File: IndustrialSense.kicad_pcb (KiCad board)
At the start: 4 copper layers, 46.9 x 90 mm, 111 parts, among them CN2 B4B-ZR (LF)(SN), CN3 ZH1.5-6P-LT, CN4 B4B-ZR (LF)(SN), J1 Conn_01x06_Socket, J3 Conn_01x06_Socket, J5 Conn_01x10_Socket, J6 Conn_01x10_Socket, Q1 SISA14DN-T1-GE3, Q13 MMBT3904, Q15 LMBT3904DW1T1G, Q2 SISA14DN-T1-GE3, Q3 SISA14DN-T1-GE3, Q4 SISA14DN-T1-GE3, Q5 CEM4435A, Q6 CH221K, SW2 SKRKAEE020, SW3 SKRKAEE020, U1 ESP32-S3-WROOM-1U-N16, U10 LM74700QDBVRQ1, U11 CN3795, U12 XFL4020-222MEC_C122469, U14 CH334F, U15 TPS3831G33DQNR, U17 THVD1406DR, U3 CH343P, U4 MAX17049G+T10, U5 LM74700QDBVRQ1, U6 LM74700QDBVRQ1, U7 TPS62132RGTT, U8 LM74700QDBVRQ1, U9 XC6209F332MR-G, X1 X322512MSB4SI

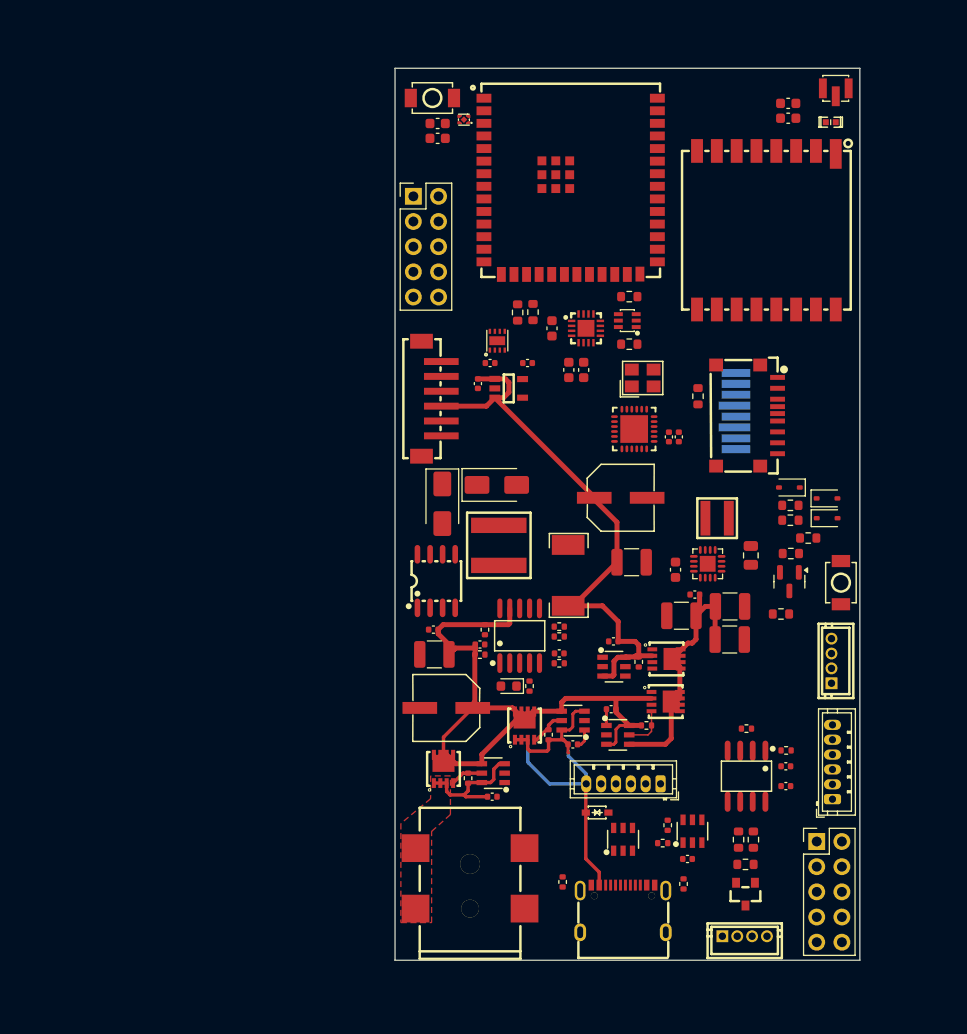
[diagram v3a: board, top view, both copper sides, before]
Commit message: [Schematic/PCB][Added] Routing almost finished
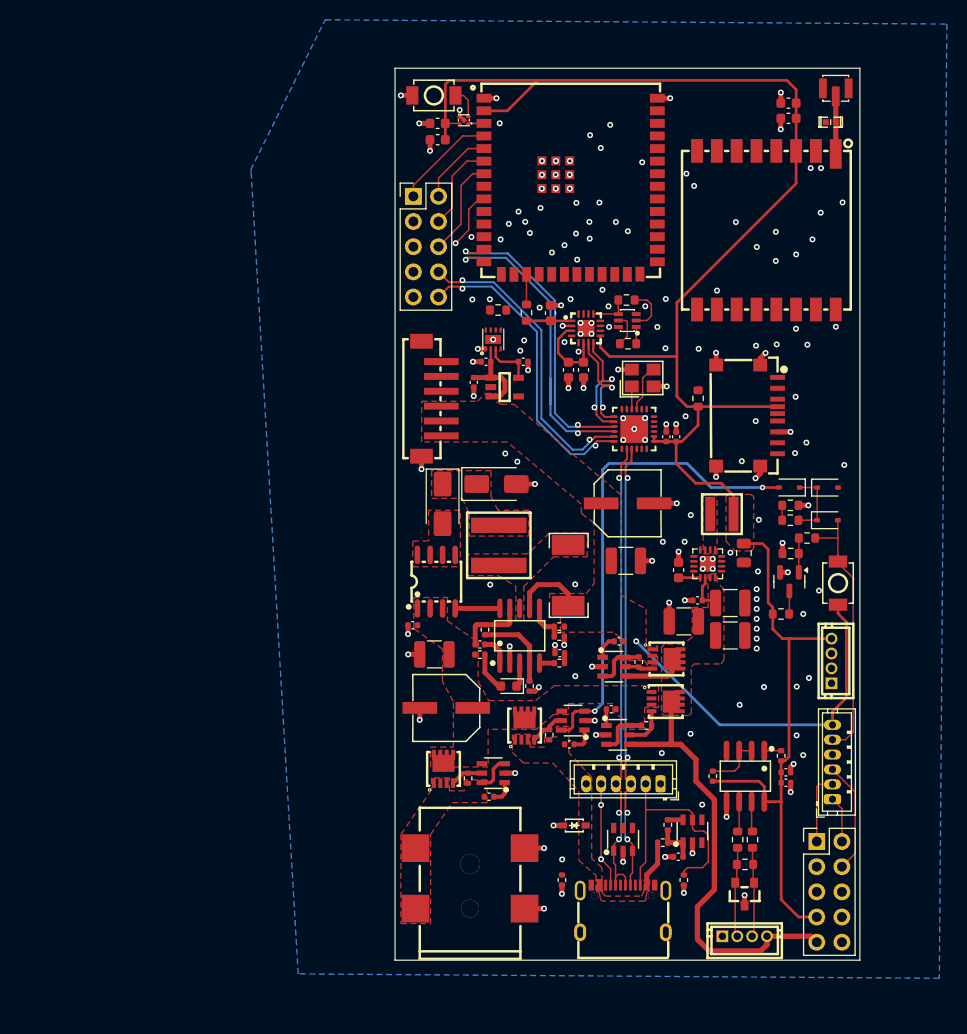
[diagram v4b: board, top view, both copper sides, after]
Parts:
- removed REF**: Micro_SD_Card, Library:microSD_card
- moved R19 5.88 mm to (156.6, 118.6), turned to 90 degrees
- moved D8 3.09 mm to (168.2, 89.5)
- moved D4 2.64 mm to (142.6, 123.6), turned to 0 degrees
- moved D7 2.20 mm to (168.1, 92.8)
- moved C22 2.13 mm to (126.3, 103.4)
- moved R58 1.99 mm to (134.9, 71.6), turned to 180 degrees
- moved C47 1.55 mm to (140.2, 71.9), turned to 90 degrees
- moved C37 0.96 mm to (153.1, 126.8), turned to 180 degrees
- moved C7 0.90 mm to (148.0, 91.1)
- moved C13 0.74 mm to (159.7, 96.1)
- moved R18 0.74 mm to (163.5, 116.6), turned to 90 degrees
- moved R57 0.66 mm to (137.8, 71.9)
- moved C15 0.65 mm to (155.0, 100.9)
- moved U12 0.63 mm to (157.5, 92.2)
- moved C6 0.62 mm to (153.7, 103.0)
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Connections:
- D7 pad 2: /Project Architecture/Power Management/KEY_PWR -> KEY_PWR
- J3 pad 5: /Project Architecture/External Connectors/PWR_KEY -> KEY_PWR
- J5 pad 3: /Project Architecture/External Connectors/PWR_KEY -> /Project Architecture/External Connectors/GPIO15
- J5 pad 5: /Project Architecture/External Connectors/GPIO15 -> /Project Architecture/External Connectors/GPIO16
- J5 pad 6: /Project Architecture/External Connectors/GPIO16 -> GND
- R48 pad 1: /Project Architecture/Power Management/KEY_PWR -> KEY_PWR
- SW2 pad 1: /Project Architecture/Power Management/KEY_PWR -> KEY_PWR
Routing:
- net 3V3_MCU: track 0.00 -> 186.0 mm
- net GND: track 0.00 -> 67.1 mm, vias 0 -> 95
- net V_CHRG: track 66.8 -> 13.0 mm
- net /Project Architecture/External Connectors/USBCD-: track 0.00 -> 47.7 mm, vias 0 -> 4
- net /Project Architecture/External Connectors/USBCD+: track 0.00 -> 45.6 mm, vias 0 -> 4
- net /Project Architecture/HUB/ESP_USBD-: track 0.00 -> 36.6 mm, vias 0 -> 2
- net /Project Architecture/HUB/ESP_USBD+: track 0.00 -> 36.6 mm, vias 0 -> 2
- net /Project Architecture/External Connectors/LTE_USBD-: track 0.00 -> 31.3 mm, vias 0 -> 2
- net /Project Architecture/External Connectors/LTE_USBD+: track 0.00 -> 31.3 mm, vias 0 -> 2
- net V_MAIN: track 26.1 -> 55.2 mm
- net KEY_PWR: track 0.00 -> 27.5 mm
- net /Project Architecture/External Connectors/CC2: track 0.00 -> 24.6 mm
- net VBUS: track 37.1 -> 53.4 mm, vias 0 -> 2
- net /Project Architecture/HUB/CH343_USBD-: track 0.00 -> 12.2 mm, vias 0 -> 2
- net /Project Architecture/HUB/CH343_USBD+: track 0.00 -> 11.4 mm, vias 0 -> 2
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- added copper zone on F.Cu, net 3V3_MCU
- added copper zone on B.Cu, net GND
- added copper zone on F.Cu, net Net-(D1-K)
- added copper zone on F.Cu, net Net-(D2-A)
- added copper zone on F.Cu, net Net-(U11-CSP)
- added copper zone on F.Cu, net Net-(U12-Pad1)
- added copper zone on F.Cu, net VBUS
- added copper zone on F.Cu, net V_BAT
- added copper zone on F.Cu, net V_CHRG
- added copper zone on F.Cu, net V_MAIN

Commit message: [Schematic/PCB][Added] Routing finished, DRC finished
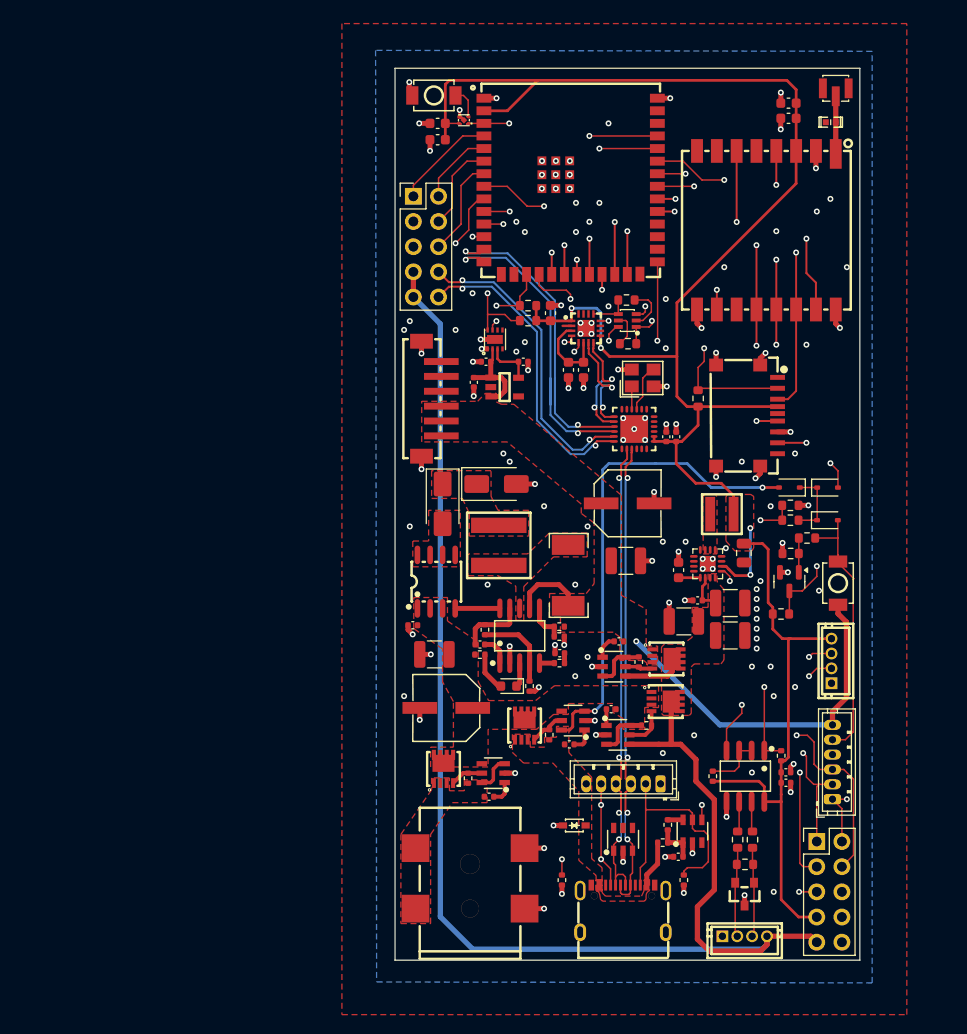
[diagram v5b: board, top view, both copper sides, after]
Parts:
- removed J1, J3: Conn_01x06_Socket, Connector_JST:JST_ZH_B6B-ZR_1x06_P1.50mm_Vertical
- added U13: B6B-ZR (LF)(SN), easyeda2kicad:CONN-TH-6P-P1.50_B6B-ZR-LF-SN, F.Cu at (147.6, 119.4)
- added U2: B6B-ZR (LF)(SN), easyeda2kicad:CONN-TH-6P-P1.50_B6B-ZR-LF-SN, F.Cu at (168.7, 117.2)
- moved R58 3.20 mm to (137.9, 72.7)
- moved R57 0.73 mm to (137.9, 71.2), turned to 180 degrees
- moved U4 0.18 mm to (134.6, 74.6)
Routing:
- net /Project Architecture/External Connectors/GPIO16: track 5.94 -> 118.2 mm, vias 1 -> 7
- net /Project Architecture/External Connectors/GPIO15: track 0.00 -> 104.6 mm, vias 2 -> 7
- net V_MAIN: track 55.2 -> 156.8 mm
- net /Project Architecture/External Connectors/I2C_SCL: track 3.04 -> 93.8 mm, vias 1 -> 7
- net /Project Architecture/External Connectors/I2C_SDA: track 0.01 -> 89.3 mm
- net /Project Architecture/MCU/RS485_RXD1: track 1.70 -> 89.8 mm
- net /Project Architecture/External Connectors/GPIO42R: track 4.66 -> 88.5 mm, vias 1 -> 4
- net /Project Architecture/External Connectors/GPIO41G: track 7.23 -> 89.1 mm, vias 6 -> 5
- net /Project Architecture/MCU/RS485_TXD1: track 0.00 -> 81.1 mm
- net /Project Architecture/External Connectors/GPIO40B: track 11.4 -> 87.6 mm, vias 4 -> 3
- net /Project Architecture/MCU/PWR_KEY: track 2.34 -> 58.6 mm, vias 0 -> 3
- net /Project Architecture/MCU/LOCK_PWR: track 0.00 -> 46.9 mm, vias 2 -> 3
- net /Project Architecture/LoRa/SPI_MISO/D0: track 0.00 -> 46.0 mm
- net /Project Architecture/LoRa/SPI_MOSI/CMD: track 0.00 -> 43.1 mm, vias 4 -> 2
- net /Project Architecture/MCU/ESP_TXD0: track 0.00 -> 43.0 mm
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- added copper zone on F.Cu, net GND

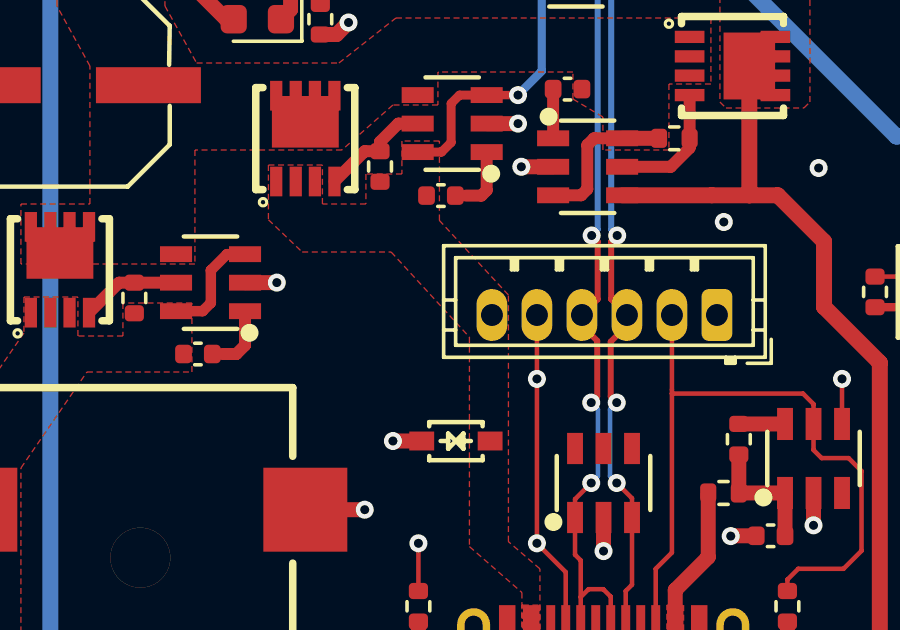
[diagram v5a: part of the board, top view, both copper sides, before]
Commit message: [Schematic/PCB][Added] Testpoints and fabrication files test
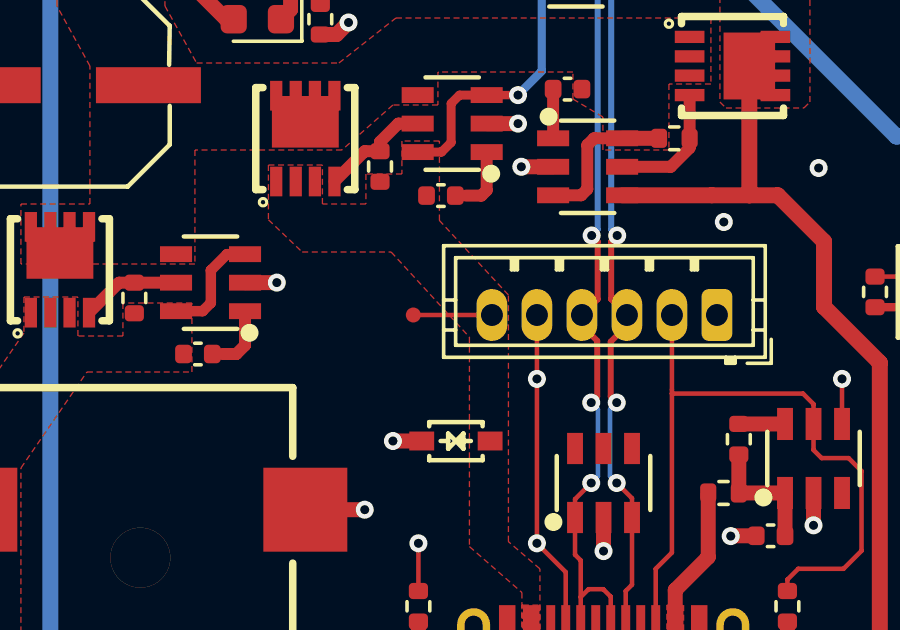
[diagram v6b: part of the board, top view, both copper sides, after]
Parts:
- added TP1: TestPoint, tests:tp05, F.Cu at (141.2, 119.4)
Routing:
- net VBUS: track 53.4 -> 56.1 mm
